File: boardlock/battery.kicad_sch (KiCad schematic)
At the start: 18 parts, among them J2 Conn_01x02_MountingPin, U4 BQ27441DRZR-G1A, U5 BQ24075RGT

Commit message: not sure what I changed
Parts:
- added J?: Conn_01x02_MountingPin, symbol Connector_Generic_MountingPin:Conn_01x02_MountingPin
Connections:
- net BATT_CHARGE_VOUT: now also J?.1 (Pin_1)
- net GND: now also J?.2 (Pin_2), J?.MP (MountPin)
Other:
- note added: "+BATT is the battery voltage after the coloumb shunt resistor"
- note added: "Babysitter Input"
- note added: "No idea what our charge timeout time is. The resistor is here so that we have the option to set it."
- note added: "Only populate if we aren't able to meet stretch PSDR"
- moved on the sheet: J2
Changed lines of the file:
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@@
   (junction (at 196.85 125.73) (diameter 0) (color 0 0 0 0)
   )
+  (junction (at 60.96 177.8) (diameter 0) (color 0 0 0 0)
+  )
   (junction (at 58.42 66.04) (diameter 0) (color 0 0 0 0)
   )
@@
   (junction (at 121.92 97.79) (diameter 0) (color 0 0 0 0)
   )
-  (junction (at 59.69 151.13) (diameter 0) (color 0 0 0 0)
+  (junction (at 60.96 143.51) (diameter 0) (color 0 0 0 0)
   )
   (junction (at 83.82 45.72) (diameter 0) (color 0 0 0 0)
@@
     (stroke (width 0) (type default))
   )
+  (wire (pts (xy 57.15 168.91) (xy 60.96 168.91))
+    (stroke (width 0) (type default))
+  )
   (wire (pts (xy 105.41 71.12) (xy 110.49 71.12))
     (stroke (width 0) (type default))
@@
     (stroke (width 0) (type default))
   )
+  (wire (pts (xy 57.15 171.45) (xy 60.96 171.45))
+    (stroke (width 0) (type default))
+  )
   (wire (pts (xy 213.36 152.4) (xy 215.9 152.4))
     (stroke (width 0) (type default))
@@
     (stroke (width 0) (type default))
   )
+  (wire (pts (xy 52.07 177.8) (xy 60.96 177.8))
+    (stroke (width 0) (type default))
+  )
   (wire (pts (xy 179.07 135.89) (xy 184.15 135.89))
     (stroke (width 0) (type default))
@@
     (stroke (width 0) (type default))
   )
+  (wire (pts (xy 60.96 171.45) (xy 60.96 177.8))
+    (stroke (width 0) (type default))
+  )
+  (wire (pts (xy 60.96 177.8) (xy 60.96 179.07))
+    (stroke (width 0) (type default))
+  )
   (wire (pts (xy 189.23 48.26) (xy 207.01 48.26))
     (stroke (width 0) (type default))
@@
     (stroke (width 0) (type default))
   )
-  (wire (pts (xy 55.88 144.78) (xy 59.69 144.78))
+  (wire (pts (xy 57.15 137.16) (xy 60.96 137.16))
     (stroke (width 0) (type default))
   )
@@
     (stroke (width 0) (type default))
   )
-  (wire (pts (xy 50.8 149.86) (xy 50.8 151.13))
+  (wire (pts (xy 52.07 142.24) (xy 52.07 143.51))
     (stroke (width 0) (type default))
   )
@@
     (stroke (width 0) (type default))
   )
+  (wire (pts (xy 52.07 176.53) (xy 52.07 177.8))
+    (stroke (width 0) (type default))
+  )
   (wire (pts (xy 184.15 130.81) (xy 184.15 135.89))
     (stroke (width 0) (type default))
@@
     (stroke (width 0) (type default))
   )
-  (wire (pts (xy 50.8 151.13) (xy 59.69 151.13))
+  (wire (pts (xy 52.07 143.51) (xy 60.96 143.51))
     (stroke (width 0) (type default))
   )
@@
     (stroke (width 0) (type default))
   )
-  (wire (pts (xy 59.69 144.78) (xy 59.69 151.13))
-    (stroke (width 0) (type default))
-  )
-  (wire (pts (xy 55.88 142.24) (xy 59.69 142.24))
+  (wire (pts (xy 60.96 137.16) (xy 60.96 143.51))
+    (stroke (width 0) (type default))
+  )
+  (wire (pts (xy 57.15 134.62) (xy 60.96 134.62))
     (stroke (width 0) (type default))
   )
@@
     (stroke (width 0) (type default))
   )
-  (wire (pts (xy 59.69 151.13) (xy 59.69 152.4))
+  (wire (pts (xy 60.96 143.51) (xy 60.96 144.78))
     (stroke (width 0) (type default))
   )
@@
     (stroke (width 0) (type default))
   )
-  (text "Battery Input" (at 35.56 134.62 0)
+  (text "Only populate if we\naren't able to meet\nstretch PSDR"
+    (at 91.44 175.26 0)
+    (effects (font (size 1.27 1.27)) (justify left bottom))
+  )
+  (text "Battery Input" (at 36.83 127 0)
     (effects (font (size 5 5) (thickness 1) bold) (justify left bottom))
   )
-  (text "+Batt is the battery\nvoltage after the\ncoloumb shunt resistor"
+  (text "+BATT is the battery\nvoltage after the\ncoloumb shunt resistor"
     (at 167.64 110.49 0)
     (effects (font (size 1.27 1.27)) (justify left bottom))
@@
     (effects (font (size 1.27 1.27)) (justify left bottom))
   )
+  (text "No idea what our charge\ntimeout time is. The\nresistor is here so that\nwe have the option to set it."
+    (at 91.44 109.22 0)
+    (effects (font (size 1.27 1.27)) (justify left bottom))
+  )
   (text "We can maybe do something\nwith these Active-Low pins\nto let the user know\nabout the charging."
     (at 144.78 92.71 0)
     (effects (font (size 1.27 1.27)) (justify left bottom))
   )
+  (text "Babysitter Input" (at 36.83 161.29 0)
+    (effects (font (size 5 5) (thickness 1) bold) (justify left bottom))
+  )
   (text "Fuel Gauge" (at 194.31 102.87 0)
     (effects (font (size 5 5) (thickness 1) bold) (justify left bottom))
@@
     (at 30.48 95.25 0)
     (effects (font (size 1.27 1.27)) (justify left bottom))
+  )
+  (global_label "BATT_CHARGE_VOUT" (shape output) (at 60.96 168.91 0) (fields_autoplaced)
+    (effects (font (size 1.27 1.27)) (justify left))
+    (property "Intersheetrefs" "${INTERSHEET_REFS}" (at 82.2695 168.91 0)
+      (effects (font (size 1.27 1.27)) (justify left) hide)
+    )
   )
   (global_label "BATT_CHARGE_EN2" (shape output) (at 146.05 40.64 0) (fields_autoplaced)
@@
     )
   )
-  (global_label "BATTERY_IN" (shape output) (at 59.69 142.24 0) (fields_autoplaced)
+  (global_label "BATTERY_IN" (shape output) (at 60.96 134.62 0) (fields_autoplaced)
     (effects (font (size 1.27 1.27)) (justify left))
-    (property "Intersheetrefs" "${INTERSHEET_REFS}" (at 73.3795 142.24 0)
+    (property "Intersheetrefs" "${INTERSHEET_REFS}" (at 74.6495 134.62 0)
       (effects (font (size 1.27 1.27)) (justify left) hide)
     )
@@
     )
   )
-  (symbol (lib_id "Connector_Generic_MountingPin:Conn_01x02_MountingPin") (at 50.8 142.24 0) (mirror y) (unit 1)
-    (in_bom yes) (on_board yes) (dnp no)
-    (property "Reference" "J2" (at 48.26 142.5956 0)
-      (effects (font (size 1.27 1.27)) (justify left))
-    )
-    (property "Value" "Conn_01x02_MountingPin" (at 48.26 145.1356 90)
+  (symbol (lib_id "Connector_Generic_MountingPin:Conn_01x02_MountingPin") (at 52.07 134.62 0) (mirror y) (unit 1)
+    (in_bom yes) (on_board yes) (dnp no)
+    (property "Reference" "J2" (at 49.53 134.9756 0)
+      (effects (font (size 1.27 1.27)) (justify left))
+    )
+    (property "Value" "Conn_01x02_MountingPin" (at 49.53 137.5156 90)
       (effects (font (size 1.27 1.27)) (justify right) hide)
     )
-    (property "Footprint" "" (at 50.8 142.24 0)
-      (effects (font (size 1.27 1.27)) hide)
-    )
-    (property "Datasheet" "~" (at 50.8 142.24 0)
+    (property "Footprint" "" (at 52.07 134.62 0)
+      (effects (font (size 1.27 1.27)) hide)
+    )
+    (property "Datasheet" "~" (at 52.07 134.62 0)
       (effects (font (size 1.27 1.27)) hide)
     )
@@
     )
   )
-  (symbol (lib_id "power:GND") (at 59.69 152.4 0) (mirror y) (unit 1)
-    (in_bom yes) (on_board yes) (dnp no)
-    (property "Reference" "#PWR035" (at 59.69 158.75 0)
-      (effects (font (size 1.27 1.27)) hide)
-    )
-    (property "Value" "GND" (at 59.69 156.21 0)
-      (effects (font (size 1.27 1.27)))
-    )
-    (property "Footprint" "" (at 59.69 152.4 0)
-      (effects (font (size 1.27 1.27)) hide)
-    )
-    (property "Datasheet" "" (at 59.69 152.4 0)
+  (symbol (lib_id "power:GND") (at 60.96 144.78 0) (mirror y) (unit 1)
+    (in_bom yes) (on_board yes) (dnp no)
+    (property "Reference" "#PWR035" (at 60.96 151.13 0)
+      (effects (font (size 1.27 1.27)) hide)
+    )
+    (property "Value" "GND" (at 60.96 148.59 0)
+      (effects (font (size 1.27 1.27)))
+    )
+    (property "Footprint" "" (at 60.96 144.78 0)
+      (effects (font (size 1.27 1.27)) hide)
+    )
+    (property "Datasheet" "" (at 60.96 144.78 0)
       (effects (font (size 1.27 1.27)) hide)
     )
@@
         (path "/e1fc29ce-837e-4062-84d8-c7e423f9eab9/a05f4dcd-7a18-4529-a05e-43353e81fbf8"
           (reference "#PWR058") (unit 1)
+        )
+      )
+    )
+  )
+  (symbol (lib_id "Connector_Generic_MountingPin:Conn_01x02_MountingPin") (at 52.07 168.91 0) (mirror y) (unit 1)
+    (in_bom yes) (on_board yes) (dnp no)
+    (property "Reference" "J?" (at 49.53 169.2656 0)
+      (effects (font (size 1.27 1.27)) (justify left))
+    )
+    (property "Value" "Conn_01x02_MountingPin" (at 49.53 171.8056 90)
+      (effects (font (size 1.27 1.27)) (justify right) hide)
+    )
+    (property "Footprint" "" (at 52.07 168.91 0)
+      (effects (font (size 1.27 1.27)) hide)
+    )
+    (property "Datasheet" "~" (at 52.07 168.91 0)
+      (effects (font (size 1.27 1.27)) hide)
+    )
+    (pin "1")
+    (pin "2")
+    (pin "MP")
+    (instances
+      (project "boardlock"
+        (path "/e1fc29ce-837e-4062-84d8-c7e423f9eab9/a05f4dcd-7a18-4529-a05e-43353e81fbf8"
+          (reference "J?") (unit 1)
         )
       )
@@
         )
       )
+    )
+  )
+  (symbol (lib_id "power:GND") (at 60.96 179.07 0) (mirror y) (unit 1)
+    (in_bom yes) (on_board yes) (dnp no)
+    (property "Reference" "#PWR024" (at 60.96 185.42 0)
+      (effects (font (size 1.27 1.27)) hide)
+    )
+    (property "Value" "GND" (at 60.96 182.88 0)
+      (effects (font (size 1.27 1.27)))
+    )
+    (property "Footprint" "" (at 60.96 179.07 0)
+      (effects (font (size 1.27 1.27)) hide)
+    )
+    (property "Datasheet" "" (at 60.96 179.07 0)
+      (effects (font (size 1.27 1.27)) hide)
+    )
+    (pin "1")
+    (instances
+      (project "boardlock"
+        (path "/e1fc29ce-837e-4062-84d8-c7e423f9eab9/a05f4dcd-7a18-4529-a05e-43353e81fbf8"
+          (reference "#PWR024") (unit 1)
+        )
+      )

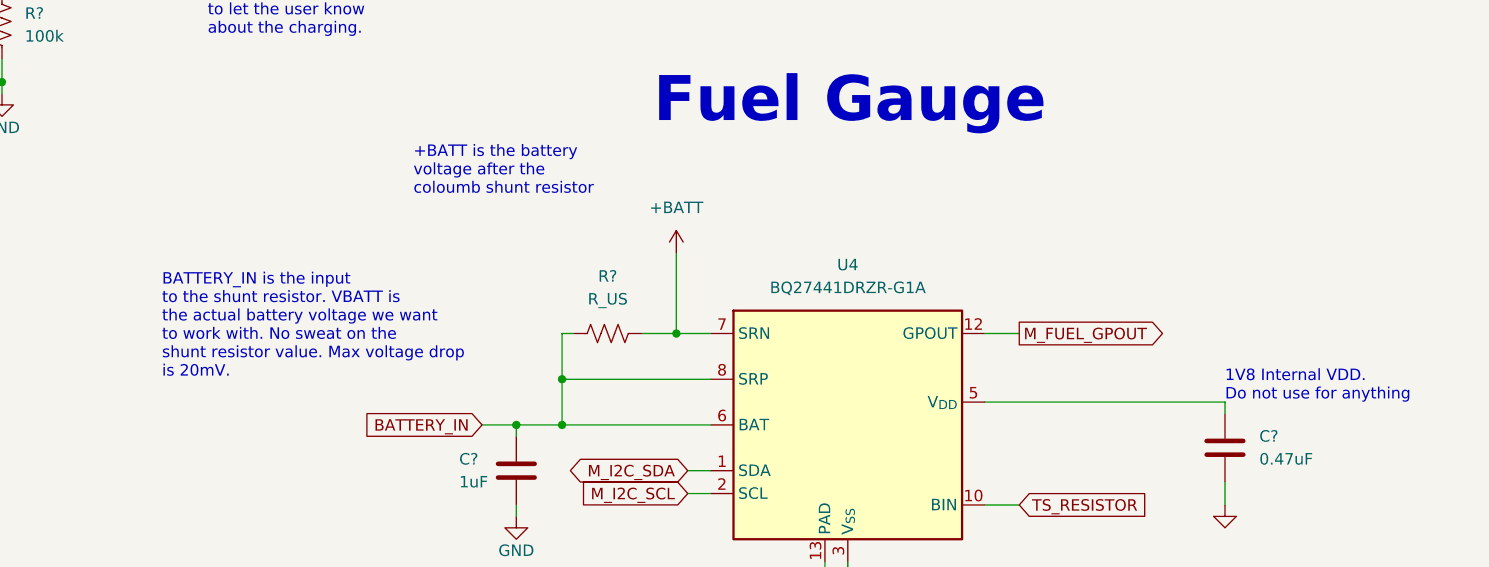
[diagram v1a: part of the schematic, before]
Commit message: continuing to add footprints
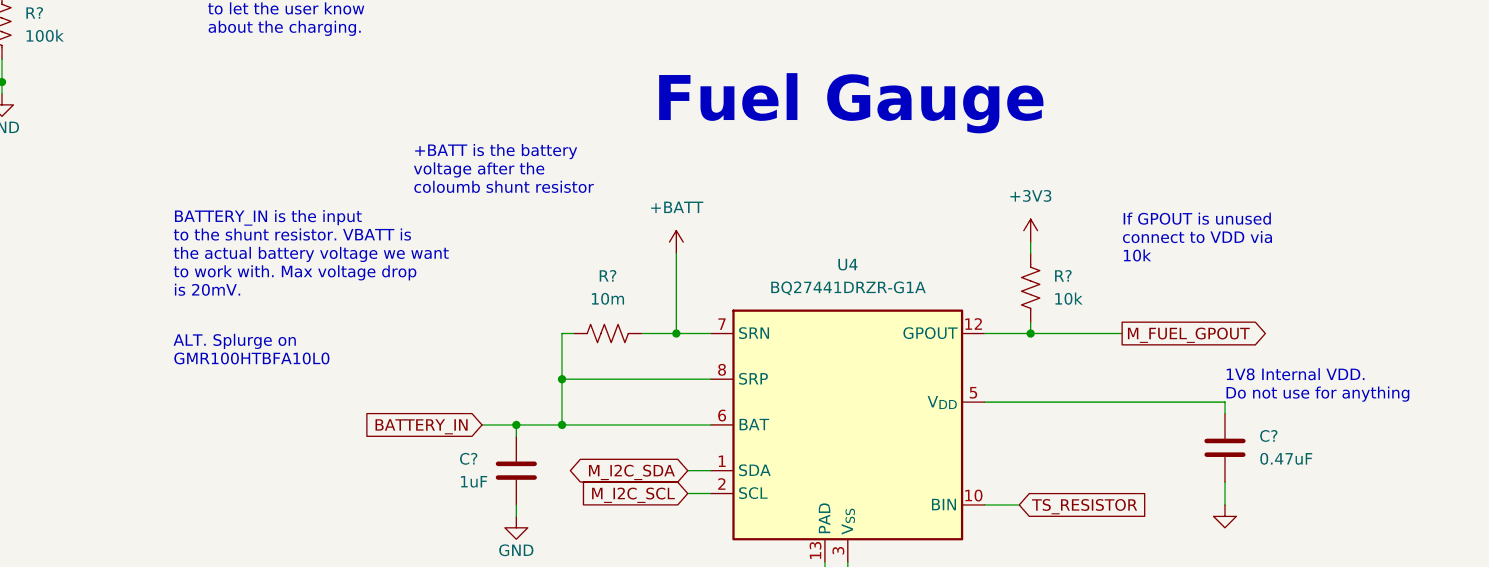
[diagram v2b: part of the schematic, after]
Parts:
- added R?: 10k, Resistor_SMD:R_0805_2012Metric_Pad1.20x1.40mm_HandSolder, symbol Device:R_US
- R? (x7): footprint (none) -> Resistor_SMD:R_0805_2012Metric_Pad1.20x1.40mm_HandSolder
- R?: value R_US -> 10m; footprint (none) -> Resistor_SMD:R_2512_6332Metric_Pad1.40x3.35mm_HandSolder; MF (none) -> Bourns Inc.; MFN (none) -> CRF2512-FZ-R010ELF; Power Rating (none) -> 2W; Tolerance (none) -> 1%; ppm drift (none) -> 50
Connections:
- net +3V3: now also R?.1
- net M_FUEL_GPOUT: now also R?.2
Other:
- note added: "ALT. Splurge on GMR100HTBFA10L0"
- note added: "BATTERY_IN is the input to the shunt resistor. VBATT is the actual battery voltage we want to work with. Max voltage drop is 20mV."
- note added: "If GPOUT is unused connect to VDD via 10k"
- note removed: "BATTERY_IN is the input to the shunt resistor. VBATT is the actual battery voltage we want to work with. No sweat on the shunt resistor value. Max voltage drop is 20mV."
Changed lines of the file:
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@@
   (junction (at 184.15 135.89) (diameter 0) (color 0 0 0 0)
   )
+  (junction (at 236.22 125.73) (diameter 0) (color 0 0 0 0)
+  )
   (junction (at 121.92 97.79) (diameter 0) (color 0 0 0 0)
   )
@@
     (stroke (width 0) (type default))
   )
+  (wire (pts (xy 236.22 124.46) (xy 236.22 125.73))
+    (stroke (width 0) (type default))
+  )
   (wire (pts (xy 57.15 168.91) (xy 60.96 168.91))
     (stroke (width 0) (type default))
@@
     (stroke (width 0) (type default))
   )
+  (wire (pts (xy 236.22 125.73) (xy 246.38 125.73))
+    (stroke (width 0) (type default))
+  )
   (wire (pts (xy 66.04 97.79) (xy 76.2 97.79))
     (stroke (width 0) (type default))
@@
     (stroke (width 0) (type default))
   )
-  (wire (pts (xy 231.14 125.73) (xy 234.95 125.73))
+  (wire (pts (xy 231.14 125.73) (xy 236.22 125.73))
     (stroke (width 0) (type default))
   )
@@
   )
   (wire (pts (xy 199.39 39.37) (xy 199.39 45.72))
+    (stroke (width 0) (type default))
+  )
+  (wire (pts (xy 236.22 115.57) (xy 236.22 116.84))
     (stroke (width 0) (type default))
   )
@@
     (effects (font (size 5 5) (thickness 1) bold) (justify left bottom))
   )
+  (text "ALT. Splurge on\nGMR100HTBFA10L0" (at 140.97 129.54 0)
+    (effects (font (size 1.27 1.27)) (justify left bottom))
+  )
   (text "Fuel Gauge" (at 194.31 102.87 0)
     (effects (font (size 5 5) (thickness 1) bold) (justify left bottom))
@@
     (effects (font (size 1.27 1.27)) (justify left bottom))
   )
+  (text "If GPOUT is unused\nconnect to VDD via\n10k" (at 246.38 118.11 0)
+    (effects (font (size 1.27 1.27)) (justify left bottom))
+  )
   (text "Charge Current\n100mA\n500mA\nISET\nStandby" (at 116.84 44.45 0)
     (effects (font (size 1.27 1.27)) (justify left bottom))
   )
-  (text "BATTERY_IN is the input\nto the shunt resistor. VBATT is\nthe actual battery voltage we want\nto work with. No sweat on the\nshunt resistor value. Max voltage drop\nis 20mV."
-    (at 139.7 130.81 0)
+  (text "BATTERY_IN is the input\nto the shunt resistor. VBATT is\nthe actual battery voltage we want\nto work with. Max voltage drop\nis 20mV."
+    (at 140.97 121.92 0)
     (effects (font (size 1.27 1.27)) (justify left bottom))
   )
@@
     )
   )
-  (global_label "M_FUEL_GPOUT" (shape output) (at 234.95 125.73 0) (fields_autoplaced)
+  (global_label "M_FUEL_GPOUT" (shape output) (at 246.38 125.73 0) (fields_autoplaced)
     (effects (font (size 1.27 1.27)) (justify left))
-    (property "Intersheetrefs" "${INTERSHEET_REFS}" (at 252.0866 125.73 0)
+    (property "Intersheetrefs" "${INTERSHEET_REFS}" (at 263.5166 125.73 0)
       (effects (font (size 1.27 1.27)) (justify left) hide)
     )
@@
       (effects (font (size 1.27 1.27)) (justify left))
     )
-    (property "Footprint" "" (at 77.216 92.964 90)
+    (property "Footprint" "Resistor_SMD:R_0805_2012Metric_Pad1.20x1.40mm_HandSolder" (at 77.216 92.964 90)
       (effects (font (size 1.27 1.27)) hide)
     )
@@
     )
   )
+  (symbol (lib_id "Device:R_US") (at 236.22 120.65 0) (unit 1)
+    (in_bom yes) (on_board yes) (dnp no) (fields_autoplaced)
+    (property "Reference" "R?" (at 238.76 119.38 0)
+      (effects (font (size 1.27 1.27)) (justify left))
+    )
+    (property "Value" "10k" (at 238.76 121.92 0)
+      (effects (font (size 1.27 1.27)) (justify left))
+    )
+    (property "Footprint" "Resistor_SMD:R_0805_2012Metric_Pad1.20x1.40mm_HandSolder" (at 237.236 120.904 90)
+      (effects (font (size 1.27 1.27)) hide)
+    )
+    (property "Datasheet" "~" (at 236.22 120.65 0)
+      (effects (font (size 1.27 1.27)) hide)
+    )
+    (pin "1")
+    (pin "2")
+    (instances
+      (project "boardlock"
+        (path "/e1fc29ce-837e-4062-84d8-c7e423f9eab9/a05f4dcd-7a18-4529-a05e-43353e81fbf8"
+          (reference "R?") (unit 1)
+        )
+        (path "/e1fc29ce-837e-4062-84d8-c7e423f9eab9"
+          (reference "R?") (unit 1)
+        )
+      )
+    )
+  )
   (symbol (lib_id "Device:C") (at 83.82 50.8 0) (unit 1)
     (in_bom yes) (on_board yes) (dnp no) (fields_autoplaced)
@@
     )
   )
+  (symbol (lib_id "power:+3V3") (at 236.22 115.57 0) (unit 1)
+    (in_bom yes) (on_board yes) (dnp no) (fields_autoplaced)
+    (property "Reference" "#PWR027" (at 236.22 119.38 0)
+      (effects (font (size 1.27 1.27)) hide)
+    )
+    (property "Value" "+3V3" (at 236.22 110.49 0)
+      (effects (font (size 1.27 1.27)))
+    )
+    (property "Footprint" "" (at 236.22 115.57 0)
+      (effects (font (size 1.27 1.27)) hide)
+    )
+    (property "Datasheet" "" (at 236.22 115.57 0)
+      (effects (font (size 1.27 1.27)) hide)
+    )
+    (pin "1")
+    (instances
+      (project "boardlock"
+        (path "/e1fc29ce-837e-4062-84d8-c7e423f9eab9/a05f4dcd-7a18-4529-a05e-43353e81fbf8"
+          (reference "#PWR027") (unit 1)
+        )
+        (path "/e1fc29ce-837e-4062-84d8-c7e423f9eab9"
+          (reference "#PWR048") (unit 1)
+        )
+      )
+    )
+  )
   (symbol (lib_id "Device:C") (at 58.42 71.12 0) (unit 1)
     (in_bom yes) (on_board yes) (dnp no) (fields_autoplaced)
@@
       (effects (font (size 1.27 1.27)))
     )
-    (property "Value" "R_US" (at 189.23 121.92 90)
-      (effects (font (size 1.27 1.27)))
-    )
-    (property "Footprint" "" (at 188.976 126.746 90)
-      (effects (font (size 1.27 1.27)) hide)
-    )
-    (property "Datasheet" "~" (at 189.23 125.73 0)
+    (property "Value" "10m" (at 189.23 121.92 90)
+      (effects (font (size 1.27 1.27)))
+    )
+    (property "Footprint" "Resistor_SMD:R_2512_6332Metric_Pad1.40x3.35mm_HandSolder" (at 188.976 126.746 90)
+      (effects (font (size 1.27 1.27)) hide)
+    )
+    (property "Datasheet" "https://www.bourns.com/docs/Product-Datasheets/CRF.pdf" (at 189.23 125.73 0)
+      (effects (font (size 1.27 1.27)) hide)
+    )
+    (property "Tolerance" "1%" (at 189.23 125.73 90)
+      (effects (font (size 1.27 1.27)) hide)
+    )
+    (property "ppm drift" "50" (at 189.23 125.73 90)
+      (effects (font (size 1.27 1.27)) hide)
+    )
+    (property "Power Rating" "2W" (at 189.23 125.73 90)
+      (effects (font (size 1.27 1.27)) hide)
+    )
+    (property "MFN" "CRF2512-FZ-R010ELF" (at 189.23 125.73 90)
+      (effects (font (size 1.27 1.27)) hide)
+    )
+    (property "MF" "Bourns Inc." (at 189.23 125.73 90)
       (effects (font (size 1.27 1.27)) hide)
     )
@@
       (effects (font (size 1.27 1.27)) (justify left))
     )
-    (property "Footprint" "" (at 211.836 65.024 90)
+    (property "Footprint" "Resistor_SMD:R_0805_2012Metric_Pad1.20x1.40mm_HandSolder" (at 211.836 65.024 90)
       (effects (font (size 1.27 1.27)) hide)
     )
@@
       (effects (font (size 1.27 1.27)) (justify left))
     )
-    (property "Footprint" "" (at 200.406 35.814 90)
+    (property "Footprint" "Resistor_SMD:R_0805_2012Metric_Pad1.20x1.40mm_HandSolder" (at 200.406 35.814 90)
       (effects (font (size 1.27 1.27)) hide)
     )
@@
       (effects (font (size 1.27 1.27)) (justify left))
     )
-    (property "Footprint" "" (at 111.506 91.694 90)
+    (property "Footprint" "Resistor_SMD:R_0805_2012Metric_Pad1.20x1.40mm_HandSolder" (at 111.506 91.694 90)
       (effects (font (size 1.27 1.27)) hide)
     )
@@
       (effects (font (size 1.27 1.27)) (justify left))
     )
-    (property "Footprint" "" (at 122.936 91.694 90)
+    (property "Footprint" "Resistor_SMD:R_0805_2012Metric_Pad1.20x1.40mm_HandSolder" (at 122.936 91.694 90)
       (effects (font (size 1.27 1.27)) hide)
     )
@@
       (effects (font (size 1.27 1.27)) (justify left))
     )
-    (property "Footprint" "" (at 190.246 35.814 90)
+    (property "Footprint" "Resistor_SMD:R_0805_2012Metric_Pad1.20x1.40mm_HandSolder" (at 190.246 35.814 90)
       (effects (font (size 1.27 1.27)) hide)
     )
@@
       (effects (font (size 1.27 1.27)) (justify left))
     )
-    (property "Footprint" "" (at 67.056 92.964 90)
-      (effects (font (size 1.27 1.27)) hide)
-    )
+    (property "Footprint" "Resistor_SMD:R_0805_2012Metric_Pad1.20x1.40mm_HandSolder" (at 67.056 92.964 90)
+      (effects (font (size 1.27 1.27)) hide)
+    )
